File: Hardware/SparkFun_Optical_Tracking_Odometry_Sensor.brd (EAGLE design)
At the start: 25.4 x 25.4 mm, 77 parts, among them J1 QWIIC_RIGHT_ANGLE, J2 QWIIC_RIGHT_ANGLE, Q1 100mA/20V/3.8Ω, Q2 100mA/20V/3.8Ω, U1 PAA5160, U2 LSM6DS0, U3 STM32C011F4U6, U4 RT9080-33GJ5

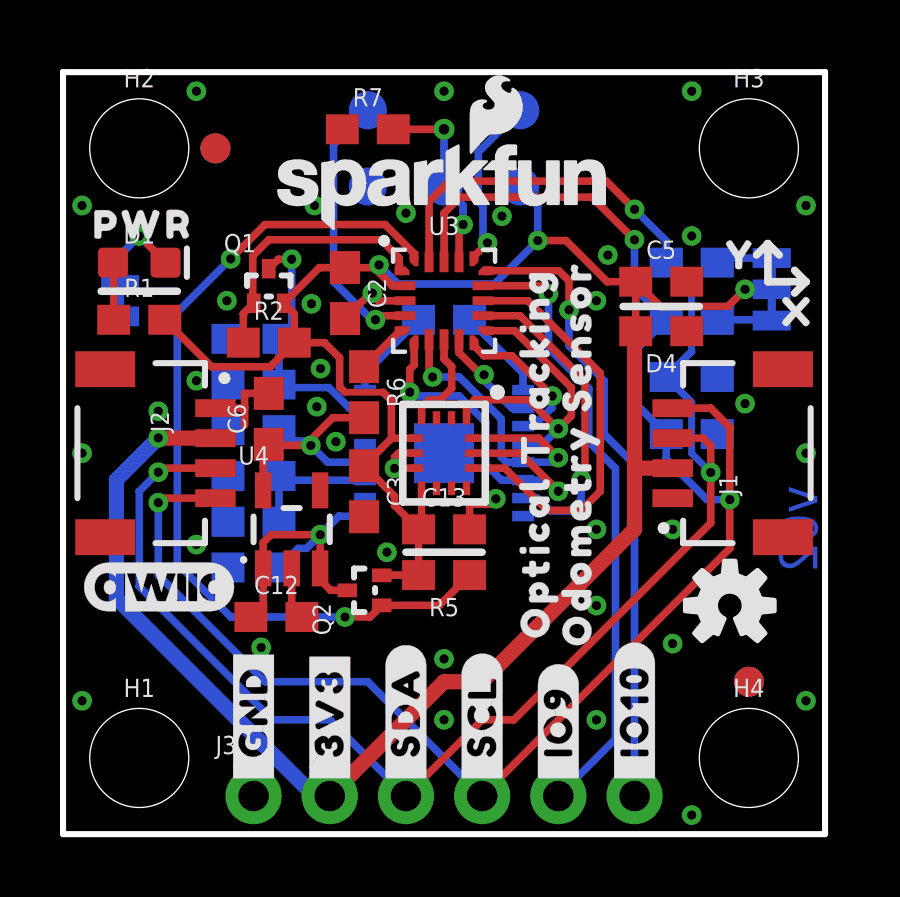
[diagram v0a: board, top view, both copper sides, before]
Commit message: v10 updates
Bump version number to v10
Add external pullup to RST net
Nudge components and traces away from mounting holes
Replace 3.3V regulator with 1.8V version
Add PROD_ID values to STM32C0 and PAA5160
Rename PAA5160 to full name of PAA5160E1-Q
Rename STM32 to STM32C011F6U6 (32kB flash version)
Swap R6 for 1k to minimize effect of leakage current into ADC
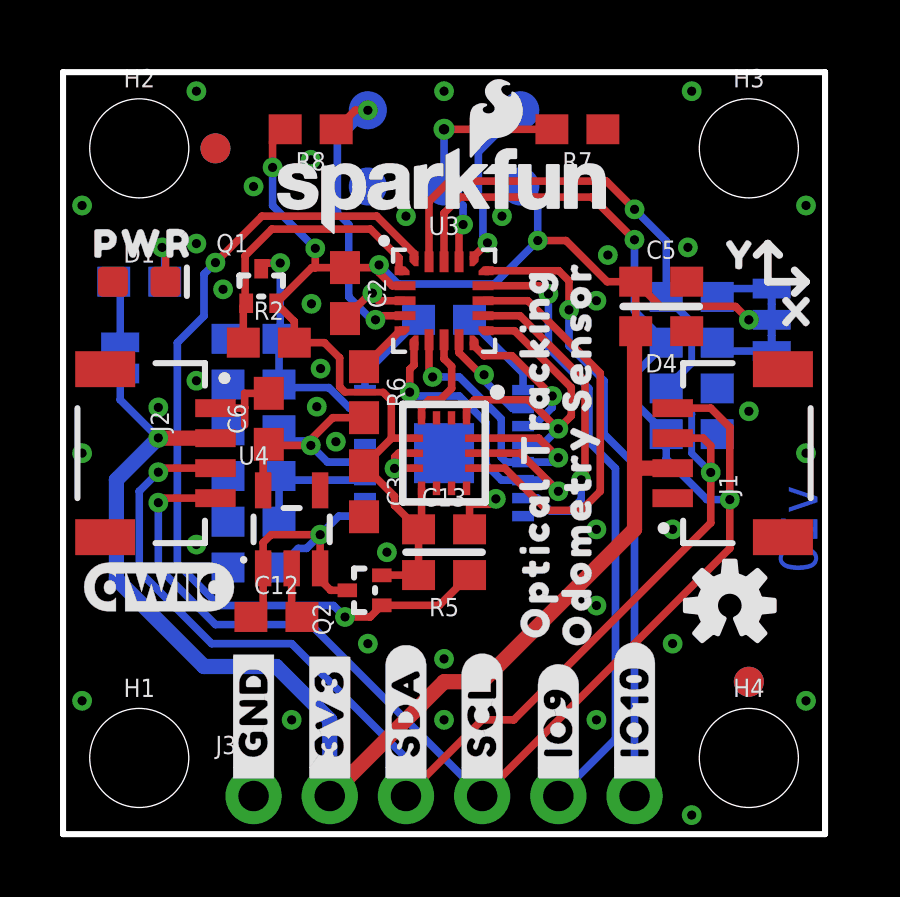
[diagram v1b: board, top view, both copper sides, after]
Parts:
- added R8: 1k, SparkFun-Resistors:0603
- R6: value 100k -> 1k
- U$1: value SWD-5PIN -> (none)
- U1: value PAA5160 -> PAA5160E1-Q; device Optical_Tracking_Odometry_Sensor:PAA5160 -> Optical_Tracking_Odometry_Sensor:PAA5160E1-Q
- U3: value STM32C011F4U6 -> STM32C011F6U6; device Optical_Tracking_Odometry_Sensor:STM32C011F4U6 -> Optical_Tracking_Odometry_Sensor:STM32C011F6U6
- U4: value RT9080-33GJ5 -> RT9080-18GJ5
- moved R7 6.98 mm to (17.1, 23.5), turned to 180 degrees
- moved PWR 1.91 mm to (1.91, 15.9), turned to 270 degrees
- moved U$20 1.90 mm to (1.91, 15.0)
- moved R1 1.27 mm to (2.54, 18.4), flipped to the bottom, turned to 180 degrees
- moved R3 1.14 mm to (21.0, 17.9)
- moved I2C 1.02 mm to (23.6, 17.1)
- moved U$26 1.02 mm to (23.6, 15.7)
- moved R4 0.76 mm to (21.0, 16.4)
- moved D1 0.64 mm to (2.54, 18.4)
- moved U$25 0.64 mm to (2.67, 19.7)
- moved U$24 0.63 mm to (2.54, 6.99)
- moved D2 0.38 mm to (21.0, 14.9)
- moved Q1 0.25 mm to (6.60, 18.8)
- moved LOGO3 0.13 mm to (12.7, 21.5)
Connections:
- net 3.3V: now also PWR.2, R8.2; no longer R1.2
- net GND: now also D1.A; no longer PWR.1
- net N$1: now also PWR.1; no longer D1.A
- net N$2: now also R1.2; no longer PWR.2
- net STM_!RST!: now also R8.1
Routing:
- net 3.3V: track 85.0 -> 89.2 mm, vias 4 -> 6
- net STM_SWCLK: track 6.42 -> 8.33 mm
- net STM_!RST!: track 9.15 -> 10.4 mm, vias 1 -> 2
- net N$2: track 3.15 -> 2.37 mm
- net GND: vias 37 -> 40
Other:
- board text added: "v10"
- board text removed: "v02"

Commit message: Replace external reset pullup with decoupling cap
Turns out the datasheet calls for it, whoops!
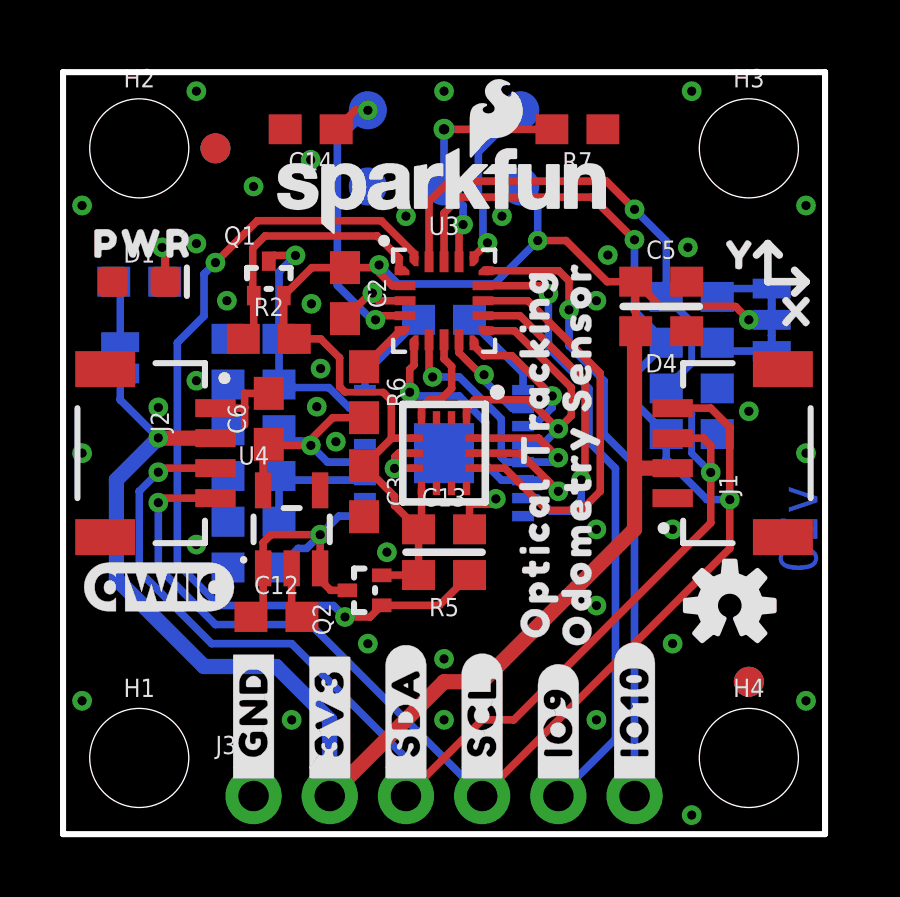
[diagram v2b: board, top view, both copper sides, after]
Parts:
- removed R8: 1k, SparkFun-Resistors:0603
- added C14: 0.1uF, SparkFun-Capacitors:0603
- moved Q1 0.36 mm to (6.86, 19.1)
- moved R2 0.13 mm to (6.86, 16.5)
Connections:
- net 3.3V: no longer R8.2
- net GND: now also C14.2
- net STM_!RST!: now also C14.1; no longer R8.1
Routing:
- net 3.3V: track 89.2 -> 83.5 mm, vias 6 -> 4
- net 3.3V_SW2: track 7.97 -> 8.69 mm
